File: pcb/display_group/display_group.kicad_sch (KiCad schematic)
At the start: 2 parts, among them J3 SELECT, J4 SEGMENTS

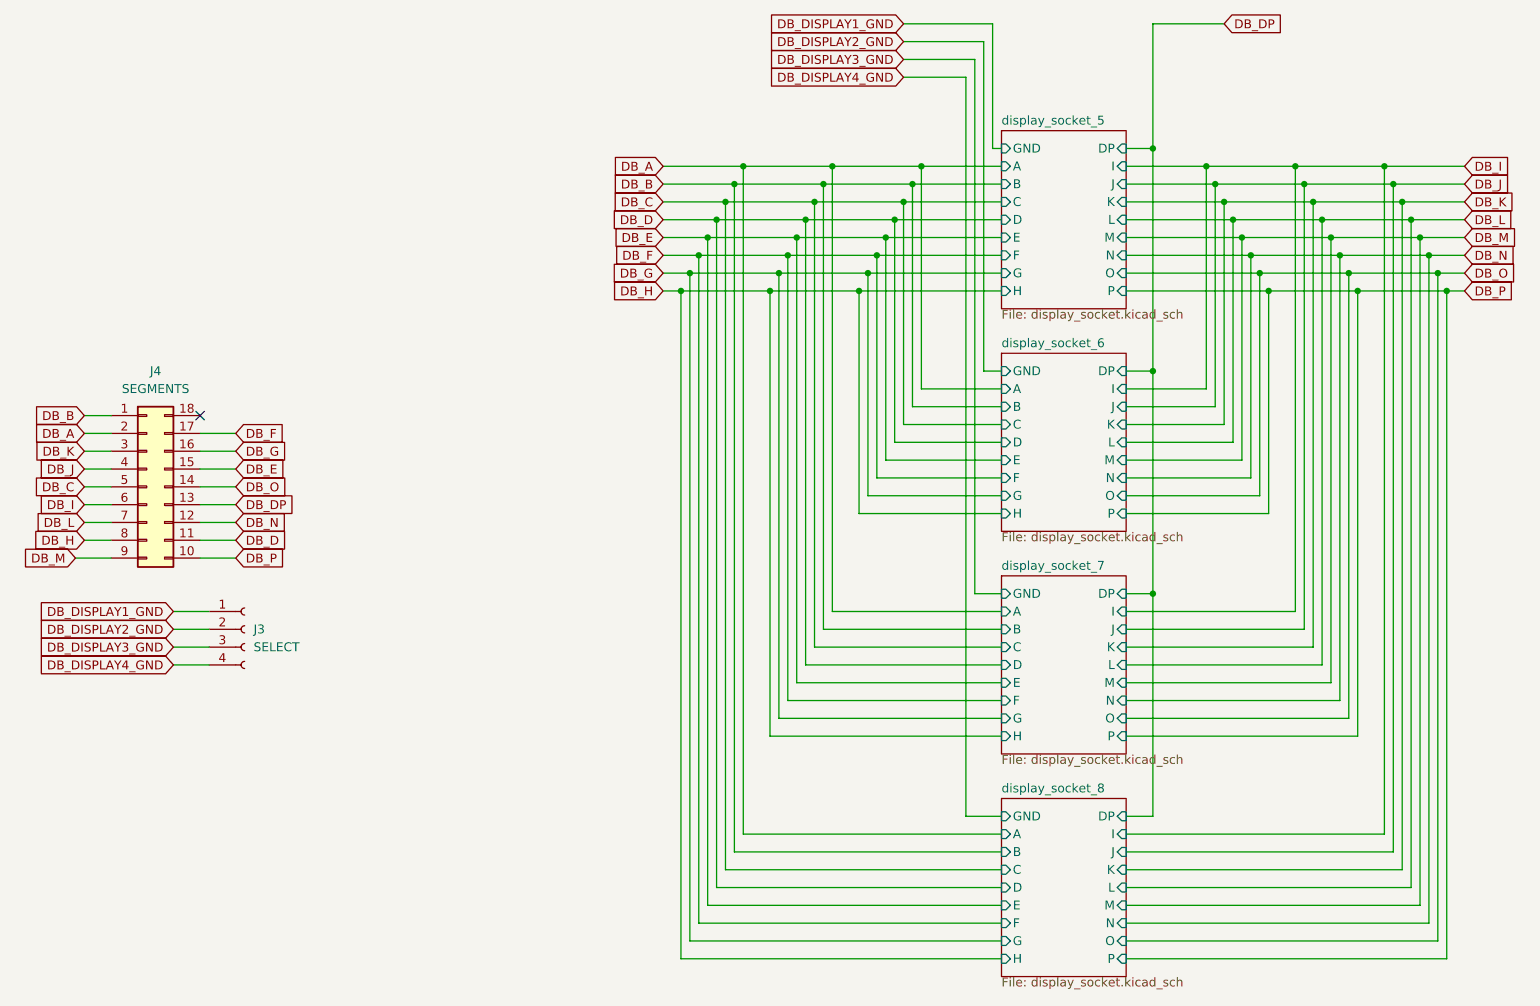
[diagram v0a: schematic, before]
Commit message: cleaned up, reworked and (so far) finalized the display-group board
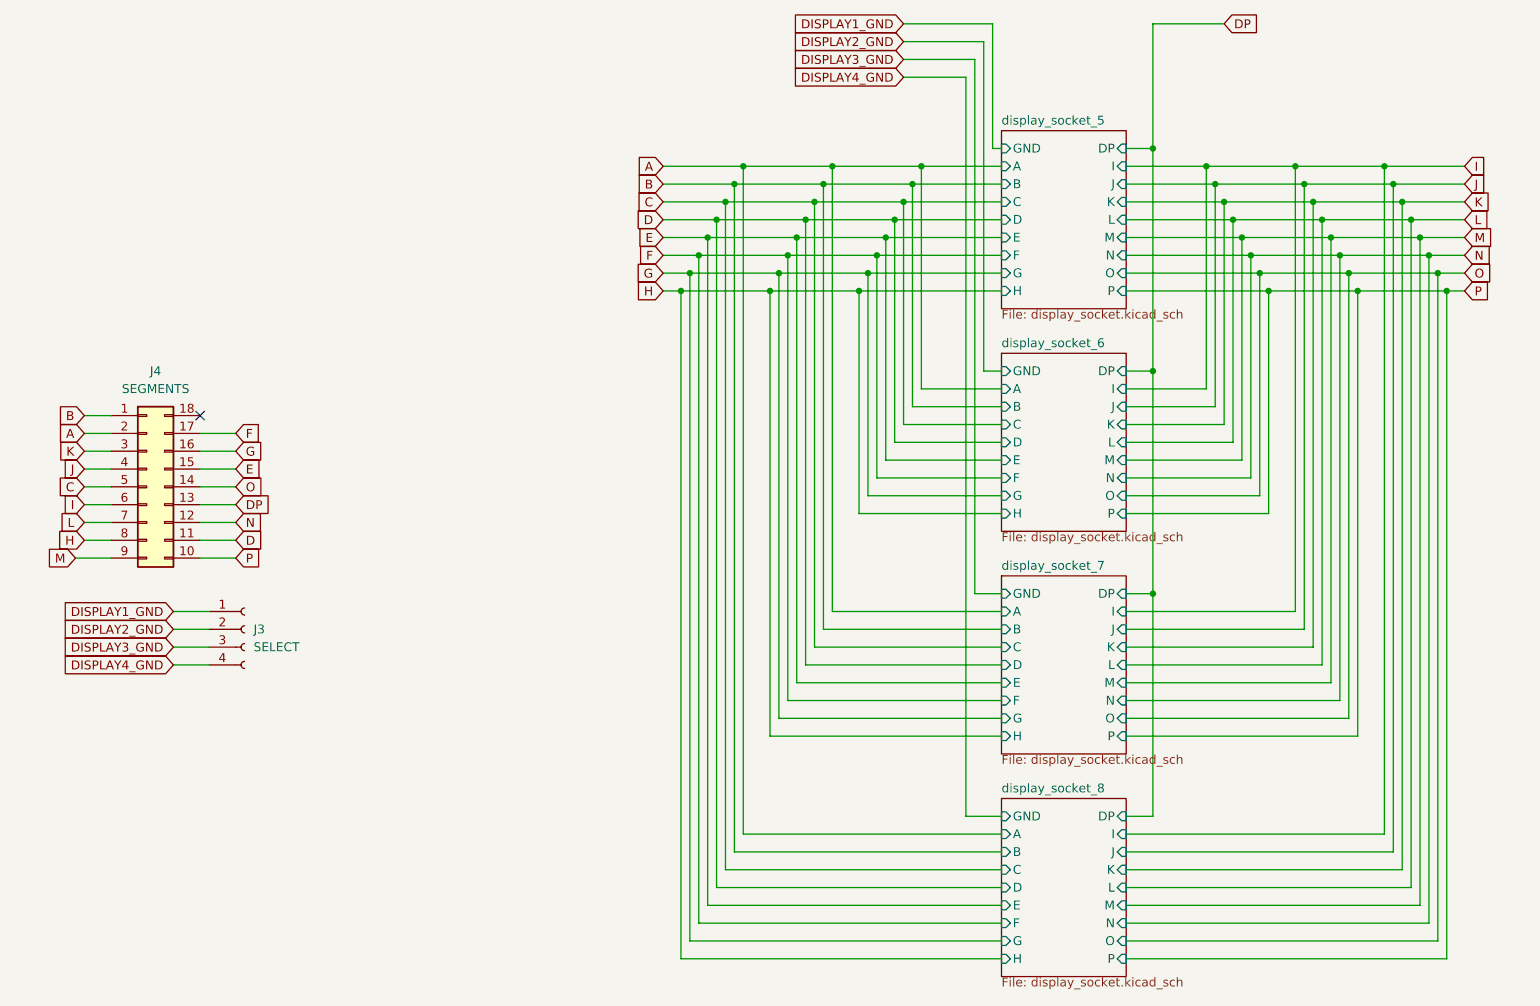
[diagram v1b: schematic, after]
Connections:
- net DB_A renamed A
- net DB_B renamed B
- net DB_C renamed C
- net DB_D renamed D
- net DB_DISPLAY1_GND renamed DISPLAY1_GND
- net DB_DISPLAY2_GND renamed DISPLAY2_GND
- net DB_DISPLAY3_GND renamed DISPLAY3_GND
- net DB_DISPLAY4_GND renamed DISPLAY4_GND
- net DB_DP renamed DP
- net DB_E renamed E
- net DB_F renamed F
- net DB_G renamed G
- net DB_H renamed H
- net DB_I renamed I
- net DB_J renamed J
- net DB_K renamed K
- net DB_L renamed L
- net DB_M renamed M
- net DB_N renamed N
- net DB_O renamed O
- net DB_P renamed P
